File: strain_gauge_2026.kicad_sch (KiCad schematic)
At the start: 22 parts, among them J2 Conn_01x04_Socket, J3 Conn_01x04_Socket, J5 Conn_01x04_Socket, U1 NAU7802SGI

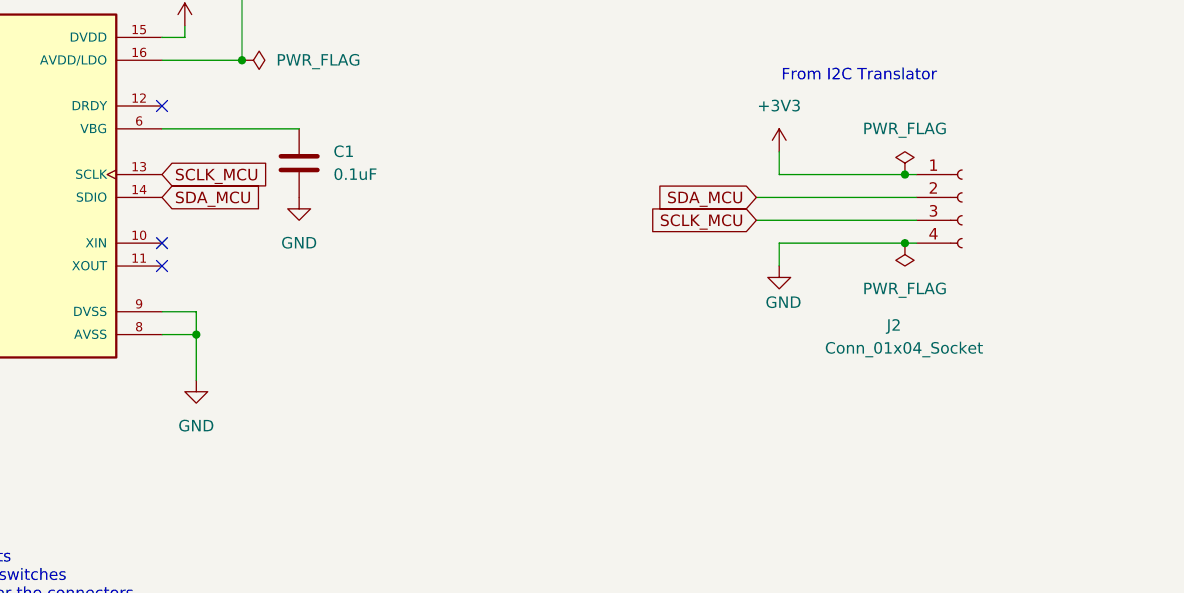
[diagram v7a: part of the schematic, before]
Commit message: Updated Connector to match i2c translator board
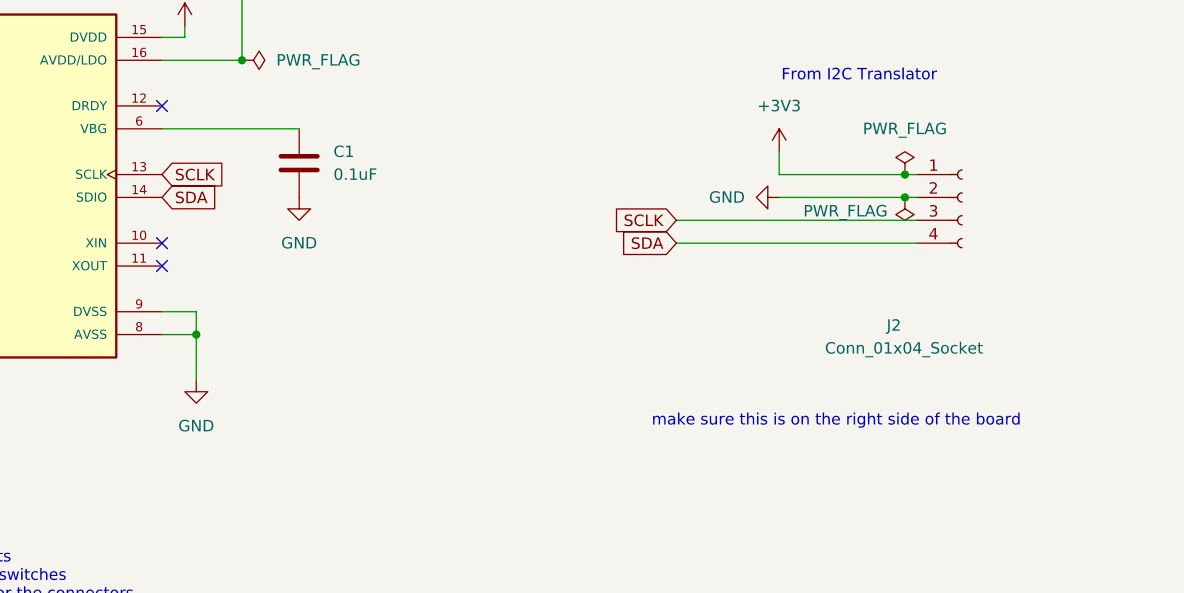
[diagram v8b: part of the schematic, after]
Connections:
- net GND: now also J2.2 (Pin_2); no longer J2.4 (Pin_4)
- net SCLK_MCU renamed SCLK
- net SDA_MCU renamed SDA
- net SDA: now also J2.4 (Pin_4); no longer J2.2 (Pin_2)
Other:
- note added: "make sure this is on the right side of the board"
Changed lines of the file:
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@@
 		)
 	)
+	(text "make sure this is on the right side of the board"
+		(exclude_from_sim no)
+		(at 247.65 120.142 0)
+		(effects
+			(font
+				(size 1.27 1.27)
+			)
+		)
+	)
 	(text "NOTE: For half bridge, solder on extra strain gauge spot,\nleave THT resistor (R3,R7) UNSOLDERED.\nLikewise for quarter bridge, solder on the THT resistor and\nleave the other strain gauge UNSOLDERED\ndo NOT solder on both at the same time!!!"
 		(exclude_from_sim no)
@@
 	)
 	(junction
-		(at 255.27 100.33)
+		(at 132.08 55.88)
 		(diameter 0)
 		(color 0 0 0 0)
 	)
 	(junction
-		(at 132.08 55.88)
+		(at 255.27 95.25)
 		(diameter 0)
 		(color 0 0 0 0)
@@
 	(wire
 		(pts
+			(xy 255.27 95.25) (xy 256.54 95.25)
+		)
+		(stroke
+			(width 0)
+			(type default)
+		)
+	)
+	(wire
+		(pts
 			(xy 33.02 45.72) (xy 39.37 45.72)
 		)
@@
 	(wire
 		(pts
-			(xy 176.53 110.49) (xy 176.53 115.57)
+			(xy 229.87 97.79) (xy 256.54 97.79)
 		)
 		(stroke
@@
 	(wire
 		(pts
-			(xy 241.3 100.33) (xy 255.27 100.33)
+			(xy 176.53 110.49) (xy 176.53 115.57)
 		)
 		(stroke
@@
 	(wire
 		(pts
-			(xy 238.76 95.25) (xy 256.54 95.25)
+			(xy 128.27 87.63) (xy 128.27 92.71)
 		)
 		(stroke
@@
 	(wire
 		(pts
-			(xy 128.27 87.63) (xy 128.27 92.71)
+			(xy 120.65 87.63) (xy 128.27 87.63)
 		)
 		(stroke
@@
 	(wire
 		(pts
-			(xy 120.65 87.63) (xy 128.27 87.63)
+			(xy 115.57 100.33) (xy 120.65 100.33)
 		)
 		(stroke
@@
 	(wire
 		(pts
-			(xy 115.57 100.33) (xy 120.65 100.33)
+			(xy 229.87 100.33) (xy 256.54 100.33)
 		)
 		(stroke
@@
 	(wire
 		(pts
-			(xy 176.53 107.95) (xy 176.53 110.49)
+			(xy 241.3 95.25) (xy 255.27 95.25)
 		)
 		(stroke
@@
 	(wire
 		(pts
-			(xy 128.27 102.87) (xy 137.16 102.87)
+			(xy 176.53 107.95) (xy 176.53 110.49)
 		)
 		(stroke
@@
 	(wire
 		(pts
-			(xy 53.34 129.54) (xy 58.42 129.54)
+			(xy 128.27 102.87) (xy 137.16 102.87)
 		)
 		(stroke
@@
 	(wire
 		(pts
-			(xy 39.37 45.72) (xy 39.37 48.26)
+			(xy 53.34 129.54) (xy 58.42 129.54)
 		)
 		(stroke
@@
 	(wire
 		(pts
-			(xy 53.34 127) (xy 53.34 129.54)
+			(xy 39.37 45.72) (xy 39.37 48.26)
 		)
 		(stroke
@@
 	(wire
 		(pts
-			(xy 52.07 45.72) (xy 57.15 45.72)
+			(xy 53.34 127) (xy 53.34 129.54)
 		)
 		(stroke
@@
 	(wire
 		(pts
-			(xy 46.99 139.7) (xy 46.99 143.51)
+			(xy 52.07 45.72) (xy 57.15 45.72)
 		)
 		(stroke
@@
 	(wire
 		(pts
-			(xy 241.3 100.33) (xy 241.3 102.87)
+			(xy 46.99 139.7) (xy 46.99 143.51)
 		)
 		(stroke
@@
 	(wire
 		(pts
-			(xy 255.27 100.33) (xy 256.54 100.33)
-		)
-		(stroke
-			(width 0)
-			(type default)
-		)
-	)
-	(wire
-		(pts
 			(xy 172.72 77.47) (xy 175.26 77.47)
 		)
@@
 	(wire
 		(pts
-			(xy 238.76 97.79) (xy 256.54 97.79)
-		)
-		(stroke
-			(width 0)
-			(type default)
-		)
-	)
-	(wire
-		(pts
 			(xy 39.37 55.88) (xy 45.72 55.88)
 		)
@@
 		)
 	)
-	(global_label "SDA_MCU"
+	(global_label "SDA"
 		(shape input)
-		(at 238.76 95.25 180)
+		(at 229.87 100.33 180)
 		(fields_autoplaced yes)
 		(effects
@@
 		)
 		(property "Intersheetrefs" "${INTERSHEET_REFS}"
-			(at 227.1872 95.25 0)
+			(at 223.3167 100.33 0)
 			(hide yes)
 			(show_name no)
@@
 		)
 	)
-	(global_label "SDA_MCU"
+	(global_label "SDA"
 		(shape input)
 		(at 172.72 95.25 0)
@@
 		)
 		(property "Intersheetrefs" "${INTERSHEET_REFS}"
-			(at 184.2928 95.25 0)
+			(at 179.2733 95.25 0)
 			(hide yes)
 			(show_name no)
@@
 		)
 	)
-	(global_label "SCLK_MCU"
+	(global_label "SCLK"
 		(shape input)
-		(at 238.76 97.79 180)
+		(at 229.87 97.79 180)
 		(fields_autoplaced yes)
 		(effects
@@
 		)
 		(property "Intersheetrefs" "${INTERSHEET_REFS}"
-			(at 225.9777 97.79 0)
+			(at 222.1072 97.79 0)
 			(hide yes)
 			(show_name no)
@@
 		)
 	)
-	(global_label "SCLK_MCU"
+	(global_label "SCLK"
 		(shape input)
 		(at 172.72 92.71 0)
@@
 		)
 		(property "Intersheetrefs" "${INTERSHEET_REFS}"
-			(at 185.5023 92.71 0)
+			(at 180.4828 92.71 0)
 			(hide yes)
 			(show_name no)
@@
 	(symbol
 		(lib_id "power:PWR_FLAG")
-		(at 255.27 100.33 180)
+		(at 255.27 95.25 180)
 		(unit 1)
 		(body_style 1)
@@
 		(in_pos_files yes)
 		(dnp no)
-		(fields_autoplaced yes)
 		(property "Reference" "#FLG04"
-			(at 255.27 102.235 0)
+			(at 255.27 97.155 0)
 			(hide yes)
 			(show_name no)
@@
 		)
 		(property "Value" "PWR_FLAG"
-			(at 255.27 105.41 0)
+			(at 248.666 96.774 0)
 			(show_name no)
 			(do_not_autoplace no)
@@
 		)
 		(property "Footprint" "Package_SO:TSSOP-28_4.4x9.7mm_P0.65mm"
-			(at 255.27 100.33 0)
+			(at 255.27 95.25 0)
 			(hide yes)
 			(show_name no)
@@
 		)
 		(property "Datasheet" ""
-			(at 255.27 100.33 0)
+			(at 255.27 95.25 0)
 			(hide yes)
 			(show_name no)
@@
 		)
 		(property "Description" "Special symbol for telling ERC where power comes from"
-			(at 255.27 100.33 0)
+			(at 255.27 95.25 0)
 			(hide yes)
 			(show_name no)
@@
 	(symbol
 		(lib_id "power:GND")
-		(at 95.25 39.37 0)
+		(at 241.3 95.25 270)
 		(unit 1)
 		(body_style 1)
@@
 		(dnp no)
 		(fields_autoplaced yes)
-		(property "Reference" "#PWR013"
-			(at 95.25 45.72 0)
+		(property "Reference" "#PWR01"
+			(at 234.95 95.25 0)
 			(hide yes)
 			(show_name no)
@@
 		)
 		(property "Value" "GND"
-			(at 95.25 44.45 0)
+			(at 237.49 95.2499 90)
 			(show_name no)
 			(do_not_autoplace no)
@@
 					(size 1.27 1.27)
 				)
+				(justify right)
 			)
 		)
 		(property "Footprint" ""
-			(at 95.25 39.37 0)
+			(at 241.3 95.25 0)
 			(hide yes)
 			(show_name no)
@@
 		)
 		(property "Datasheet" ""
-			(at 95.25 39.37 0)
+			(at 241.3 95.25 0)
 			(hide yes)
 			(show_name no)
@@
 		)
 		(property "Description" "Power symbol creates a global label with name \"GND\" , ground"
-			(at 95.25 39.37 0)
+			(at 241.3 95.25 0)
 			(hide yes)
 			(show_name no)
@@
 			(project "strain_gauge_2026"
 				(path "/5a10e1a7-6a1b-4f11-a3d3-893ec92bfd42"
-					(reference "#PWR013")
+					(reference "#PWR01")
 					(unit 1)
 				)
@@
 	(symbol
 		(lib_id "power:GND")
-		(at 45.72 59.69 0)
+		(at 95.25 39.37 0)
 		(unit 1)
 		(body_style 1)
@@
 		(dnp no)
 		(fields_autoplaced yes)
-		(property "Reference" "#PWR05"
-			(at 45.72 66.04 0)
+		(property "Reference" "#PWR013"
+			(at 95.25 45.72 0)
 			(hide yes)
 			(show_name no)
@@
 		)
 		(property "Value" "GND"
-			(at 45.72 64.77 0)
+			(at 95.25 44.45 0)
 			(show_name no)
 			(do_not_autoplace no)
@@
 		)
 		(property "Footprint" ""
-			(at 45.72 59.69 0)
+			(at 95.25 39.37 0)
 			(hide yes)
 			(show_name no)
@@
 		)
 		(property "Datasheet" ""
-			(at 45.72 59.69 0)
+			(at 95.25 39.37 0)
 			(hide yes)
 			(show_name no)
@@
 		)
 		(property "Description" "Power symbol creates a global label with name \"GND\" , ground"
-			(at 45.72 59.69 0)
+			(at 95.25 39.37 0)
 			(hide yes)
 			(show_name no)
@@
 			(project "strain_gauge_2026"
 				(path "/5a10e1a7-6a1b-4f11-a3d3-893ec92bfd42"
-					(reference "#PWR05")
+					(reference "#PWR013")
 					(unit 1)
 				)
@@
 	(symbol
 		(lib_id "power:GND")
-		(at 241.3 102.87 0)
+		(at 45.72 59.69 0)
 		(unit 1)
 		(body_style 1)
@@
 		(in_pos_files yes)
 		(dnp no)
-		(property "Reference" "#PWR09"
-			(at 241.3 109.22 0)
+		(fields_autoplaced yes)
+		(property "Reference" "#PWR05"
+			(at 45.72 66.04 0)
 			(hide yes)
 			(show_name no)
@@
 		)
 		(property "Value" "GND"
-			(at 239.776 106.934 0)
+			(at 45.72 64.77 0)
 			(show_name no)
 			(do_not_autoplace no)
@@
 					(size 1.27 1.27)
 				)
-				(justify left)
 			)
 		)
 		(property "Footprint" ""
-			(at 241.3 102.87 0)
+			(at 45.72 59.69 0)
 			(hide yes)
 			(show_name no)
@@
 		)
 		(property "Datasheet" ""
-			(at 241.3 102.87 0)
+			(at 45.72 59.69 0)
 			(hide yes)
 			(show_name no)
@@
 		)
 		(property "Description" "Power symbol creates a global label with name \"GND\" , ground"
-			(at 241.3 102.87 0)
+			(at 45.72 59.69 0)
 			(hide yes)
 			(show_name no)
@@
 			(project "strain_gauge_2026"
 				(path "/5a10e1a7-6a1b-4f11-a3d3-893ec92bfd42"
-					(reference "#PWR09")
+					(reference "#PWR05")
 					(unit 1)
 				)
